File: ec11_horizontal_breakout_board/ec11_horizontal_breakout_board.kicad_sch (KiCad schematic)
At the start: 6 parts, among them J1 Conn_01x01_Socket, J2 Conn_01x01_Socket, J3 Conn_01x01_Socket, J4 Conn_01x01_Socket, J50 JST-SH-4, SW3 RotaryEncoder_Switch

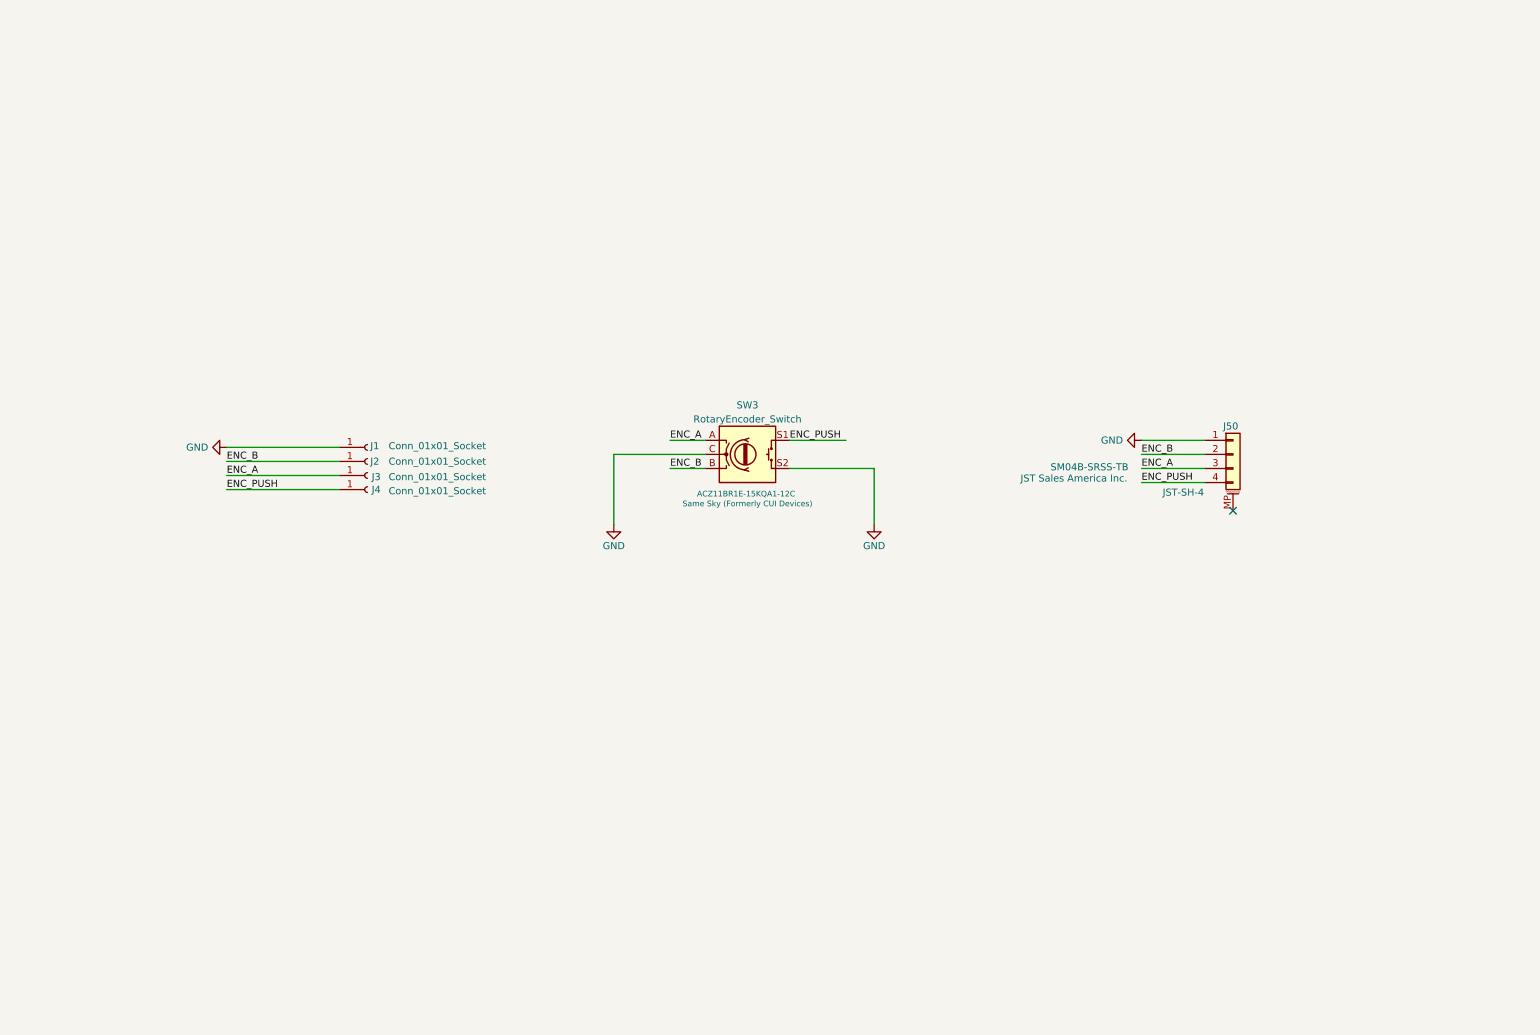
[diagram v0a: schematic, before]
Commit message: Add filtering to ec11 encoder breakout. Also change to makefile builder
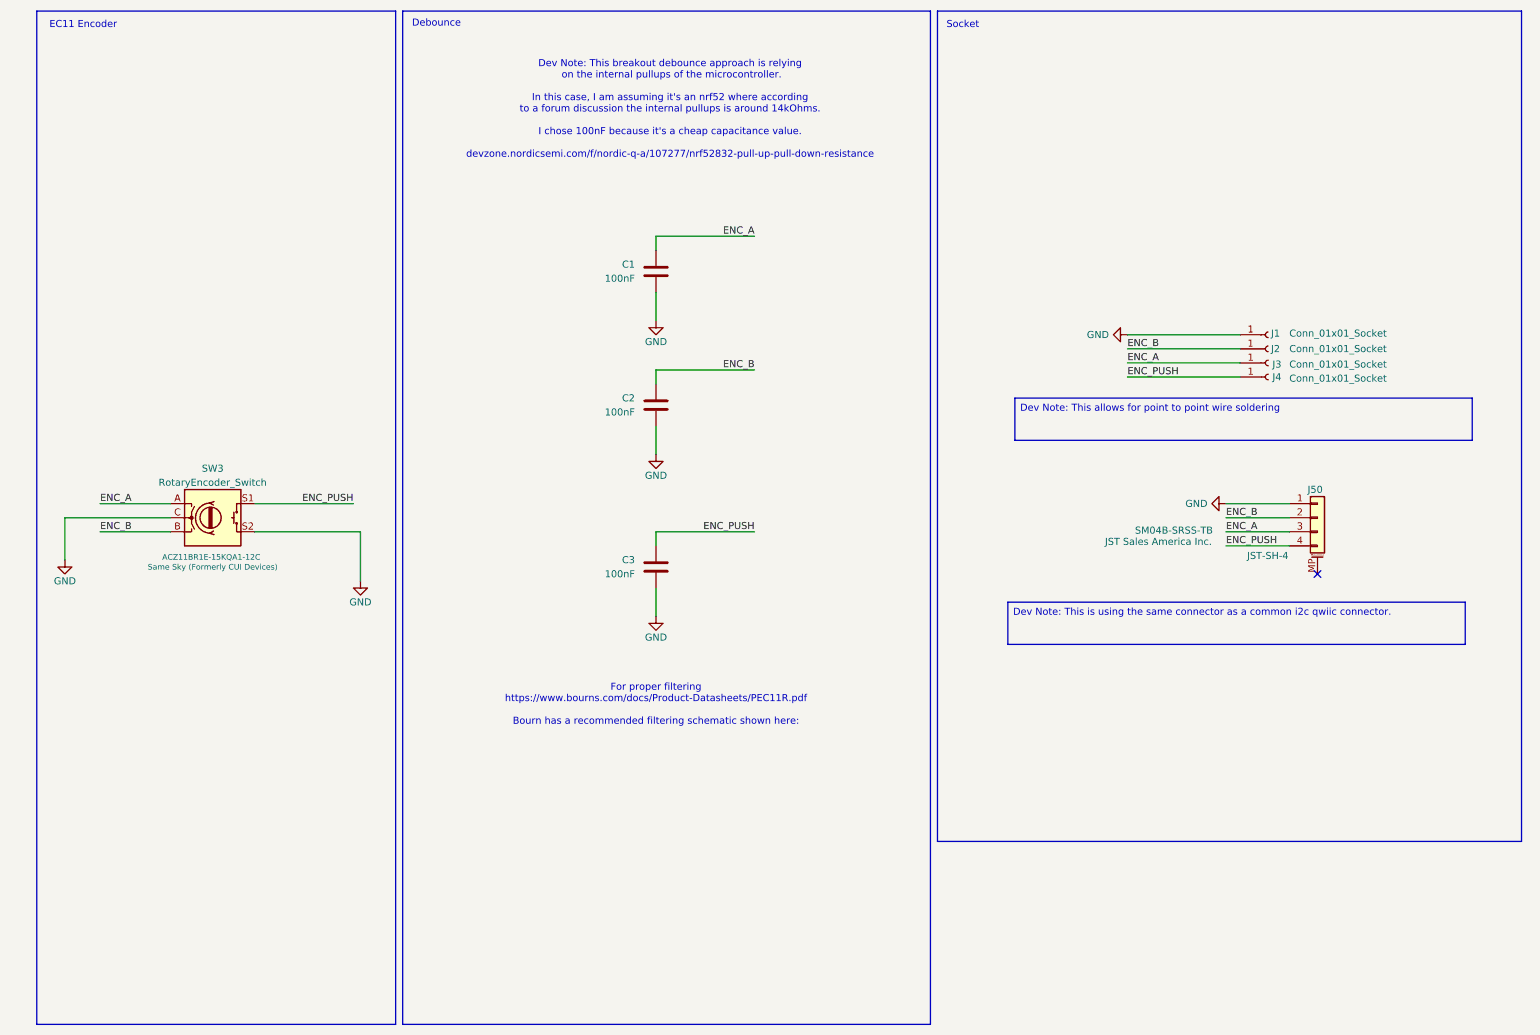
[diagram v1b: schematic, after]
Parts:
- added C1, C2, C3: 100nF, Capacitor_SMD:C_0805_2012Metric_Pad1.18x1.45mm_HandSolder, symbol Device:C
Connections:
- net ENC_A: now also C1.1
- net ENC_B: now also C2.1
- net ENC_PUSH: now also C3.1
- net GND: now also C1.2, C2.2, C3.2
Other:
- note added: "Debounce"
- note added: "Dev Note: This breakout debounce approach is relying on the internal pullups of the microcontroller. In this case, I am assuming it's an nrf52 where according to a forum discussion the internal pullups is around 14kOhms. I chose 100nF because it's a cheap capacitance value. devzone.nordicsemi.com/f/nordic-q-a/107277/nrf52832-pull-up-pull-down-resistance"
- note added: "EC11 Encoder"
- note added: "For proper filtering https://www.bourns.com/docs/Product-Datasheets/PEC11R.pdf Bourn has a recommended filtering schematic shown here:"
- note added: "Socket"
- moved on the sheet: J1, J2, J3, J4, J50, SW3

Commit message: Ec11 breakout encoder Rev3
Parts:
- removed C3: 100nF, Capacitor_SMD:C_0805_2012Metric_Pad1.18x1.45mm_HandSolder, symbol Device:C
- added R1, R2: 1K, EC11:R_0805_2012Metric_Pad1.20x1.40mm_HandSolder_And_Jumper, symbol PCM_SL_Resistors:Resistor
- added Rpullup1, Rpullup2, Rpullup3: 14K, Resistor_SMD:R_0805_2012Metric_Pad1.20x1.40mm_HandSolder, symbol PCM_SL_Resistors:Resistor
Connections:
- net ENC_A: now also R1.1; no longer C1.1, J3.1 (Pin_1), J50.3 (Pin_3)
- net ENC_B: now also R2.1; no longer C2.1, J2.1 (Pin_1), J50.2 (Pin_2)
- net ENC_PUSH: now also Rpullup3.1
- net GND: now also J50.MP (MountPin)
- new net +3.3V: Rpullup1.2, Rpullup2.2, Rpullup3.2
- new net A: C1.1, J3.1 (Pin_1), J50.3 (Pin_3), R1.2, Rpullup1.1
- new net B: C2.1, J2.1 (Pin_1), J50.2 (Pin_2), R2.2, Rpullup2.1
- no-connect marks 1 -> 0
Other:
- note added: "Implied MCU Pullups"
- moved on the sheet: C1, C2, J1, J2, J3, J4, SW3
